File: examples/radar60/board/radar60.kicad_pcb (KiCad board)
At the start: 6 copper layers, 60 x 46 mm, 6 parts

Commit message: radar60 board: Rev A integration, placed by yapnr's Monte Carlo search, not routed
integrate.py combines the schematic's atopile board, the RF macro (rfm1-n) and the floorplan,
runs pnr.mc.halving stage 0 (32 seeded starts), selects mechanically (legal, placement audit,
then the engine's routability proxy, HPWL, id) and writes the board back without routes.
kicad_ops.py merges the macro in U1's frame (copper digest equal to the RF track's board, RF
balls on the macro ports to 0 um), drops the engine's all-layer copper keepouts and the plane
drops writeback adds on its own, and fills the zones; audit.py checks R2, R4, R5, the noise
distances, regions and groups. reva/placement.json records the selected poses; the placed
board (1.2 MB, over the 600 kB limit) is rebuilt from it bit for bit.

Floorplan changes, all derived: RF region, guard and patches follow the calibrated macro; the
VOUT_PA caps go on the bottom under the corner (the macro's pocket holds no 0402 courtyard);
crystal region and HF/bulk decoupling radii widened to what U1's courtyard allows; PMIC block
and J3 region widened; the four mounting holes are the schematic's parts; keepout polygons as
point lists (they were strings) and less U1's courtyard; net classes by pattern in the project.

Co-Authored-By: Claude Opus 5.5 <noreply@anthropic.com>
Claude-Session: https://claude.ai/code/session_014FiHUDEn5jCP4V8pPjQkPy
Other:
- board text added: "pa_corner"
- board text removed: "pa_pocket"

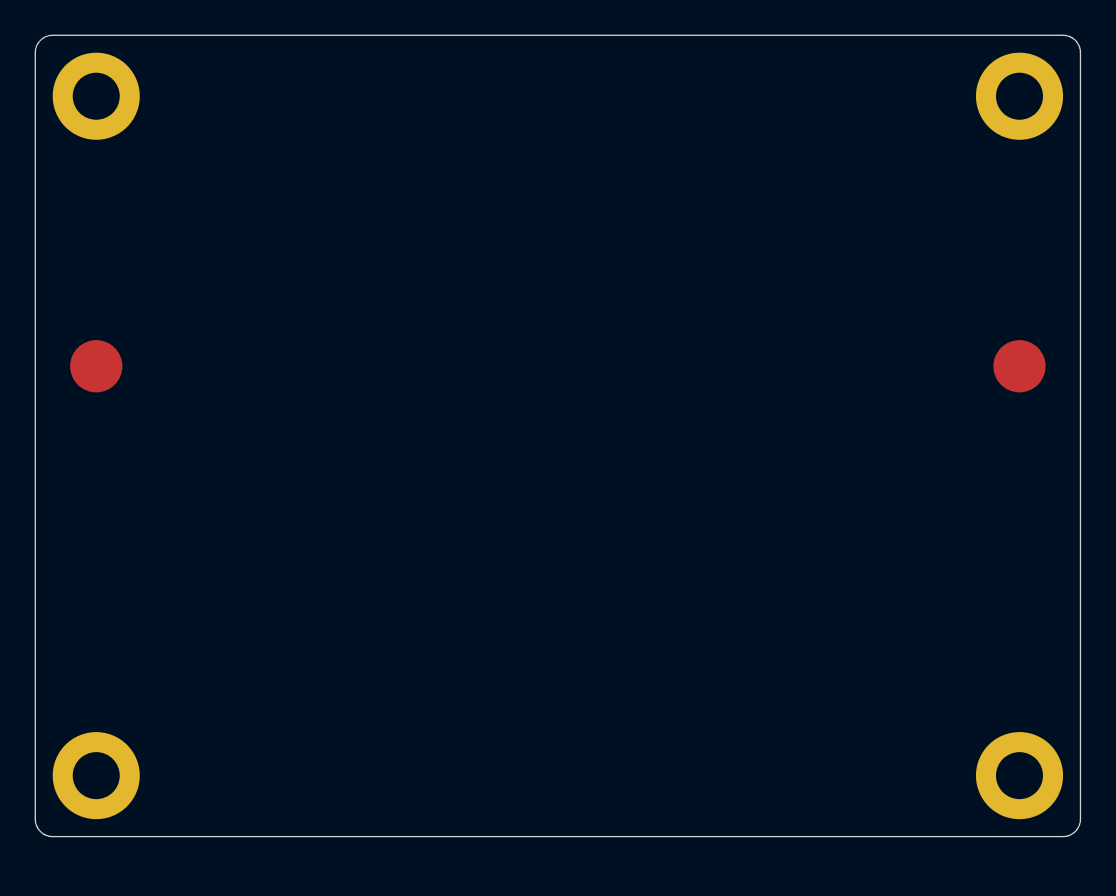
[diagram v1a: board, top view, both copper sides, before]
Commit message: radar60 board: review fixes, ball-anchored decoupling, block groups, re-placed
Adversarial reviews of 735327c (schematic/power and RF/floorplan), fixed on the board side:
- R4: net class ANALOG (VOUT_14*, VBGAP, the eFuse threshold/timer nodes, VIO_LS_ON, DAMP_*,
  PMIC_FB_B2), exempt from radar60_rf_guard_digital like RF/PWR/GND; audit.py and the derived R4
  region now use the rule's own class test (they disagreed on 11 parts). dru_selftest 21/21.
- Ball-anchored parts: U1 is fixed, so the APLL, VBGAP and SYNTH caps, the crystal load caps,
  the VOUT_PA/VIN_13RF2 220 nF and PA 0 ohm (bottom, under the corner) and the QSPI clock
  resistor each get a one-slot region next to their ball and a rotation that turns the signal
  pad toward it: 2.25/3.44/3.07, 2.1/2.3, 0.5-1.1 and 2.1 mm (were up to 12-17 mm). The PA/RF2
  bulk goes on the bottom east of the package (7-12 mm; nearer needs the BGA shadow and E4).
- Blocks: hard groups for the eFuse network, CAN and flash parts, PMIC input caps, snubbers
  (each C within 2.5 mm of its R) and VANA; regions for the block anchors and for the ESD/TVS at
  J1. J2 and J3 are fixed (as region parts the legalizer stranded them behind the blocks).
  audit.py adds pad-to-ball limits and the protection order on J1's lines.
- Outline 60 x 46.3 mm (5.0 mm ground beyond the RX patches); plated GND mounting holes at
  y 42.8; IHLP-1616 inductors in the PMIC block; BGA via rules leave the macro's RF-region vias
  to their own class; gen_board --macro checks all three D12 variants; integrate.py
  --macro-variant.

Re-placed with pnr.mc.halving stage 0 (32 starts, seed 0): 12 legal, all pass the audit,
winner p002 (no unreachable branch). KiCad DRC on the written board: only the unconfigured
footprint libraries (183) and the 432 unrouted connections. finish --placement rebuilds it bit
for bit (sha256 1d342ef4...).

Co-Authored-By: Claude Opus 5.5 <noreply@anthropic.com>
Claude-Session: https://claude.ai/code/session_014FiHUDEn5jCP4V8pPjQkPy
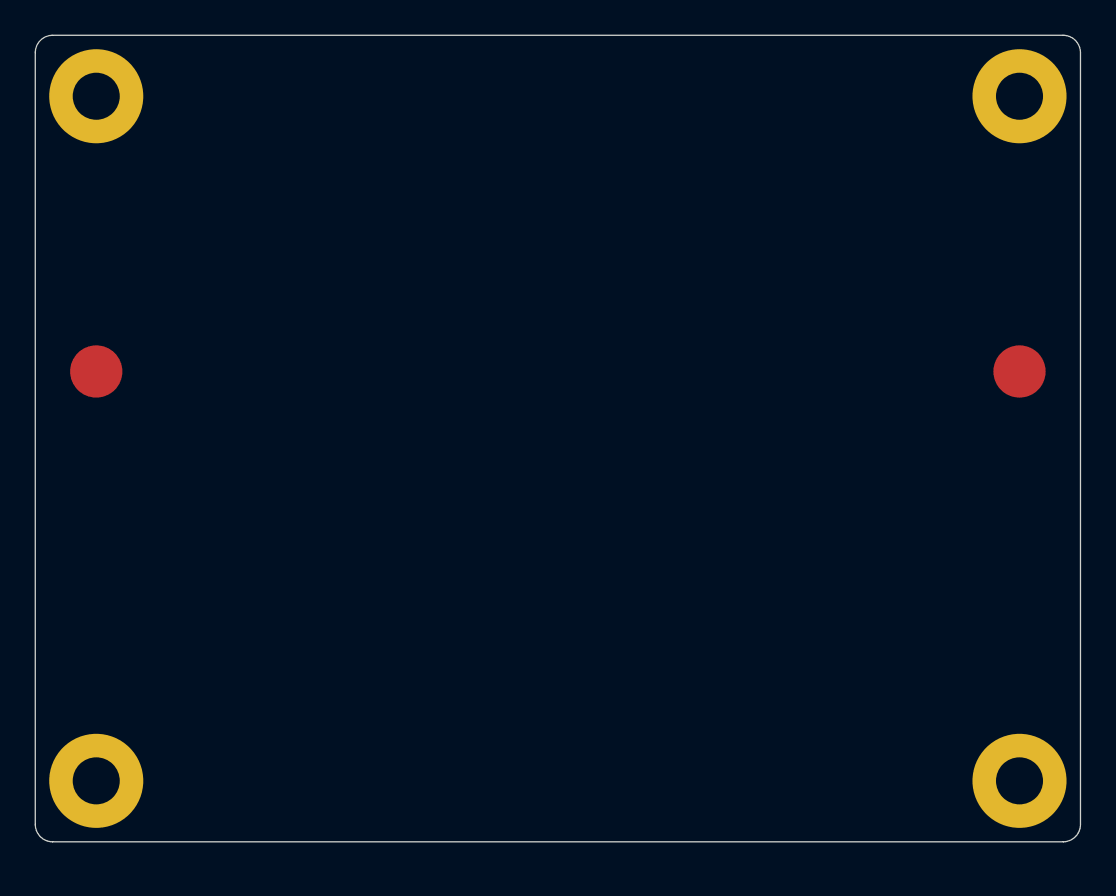
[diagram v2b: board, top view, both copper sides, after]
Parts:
- moved H1 0.30 mm to (33.5, 72.8)
- moved H2 0.30 mm to (86.5, 72.8)
- moved RL1 0.30 mm to (33.5, 49.3)
- moved RL2 0.30 mm to (86.5, 49.3)
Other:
- board size 60 x 46 mm -> 60 x 46.3 mm
- board text added: "can_block"
- board text added: "connector_esd"
- board text added: "connector_tvs"
- board text added: "efuse_block"
- board text added: "flash_block"
- board text added: "pa_bulk"
- board text added: "pa_cap"
- board text added: "pa_r"
- board text added: "qspi_series"
- board text added: "radio_apll"
- board text added: "radio_synth"
- board text added: "radio_vbgap"
- board text added: "radio_west"
- board text added: "rf2_cap"
- board text added: "xtal_cap_n"
- board text added: "xtal_cap_p"
- board text removed: "jtag"
- board text removed: "lvds_header"
- board text removed: "pa_corner"

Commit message: radar60 board: floorplan from the RF macro's board_frame
The RF-uniformity macro put 473 vias and the new TX bank outside the
floorplan's RF region, so `gen_board.py --check --macro` failed. The
floorplan now takes its values from the macro's board_frame:

- board 60 x 47.35 mm, with the top mounting holes at y 43.85;
- the RF region x 12.599-51.469 and the R4 guard x 7.599-56.469;
- the patch extents including the dummy columns;
- the VOUT_PA pocket 29.557-31.25 x 33.2-34.2 (it holds no part; the
  VOUT_PA parts stay on the bottom side).

constraints.yaml and radar60.kicad_pcb are regenerated, and
`gen_board.py --check --macro --compile` passes for rfm1-m/n/p.
reva/ (the placed board) is still the old macro's; stage 3 re-places it.

Co-Authored-By: Claude Opus 5.5 <noreply@anthropic.com>
Claude-Session: https://claude.ai/code/session_014FiHUDEn5jCP4V8pPjQkPy
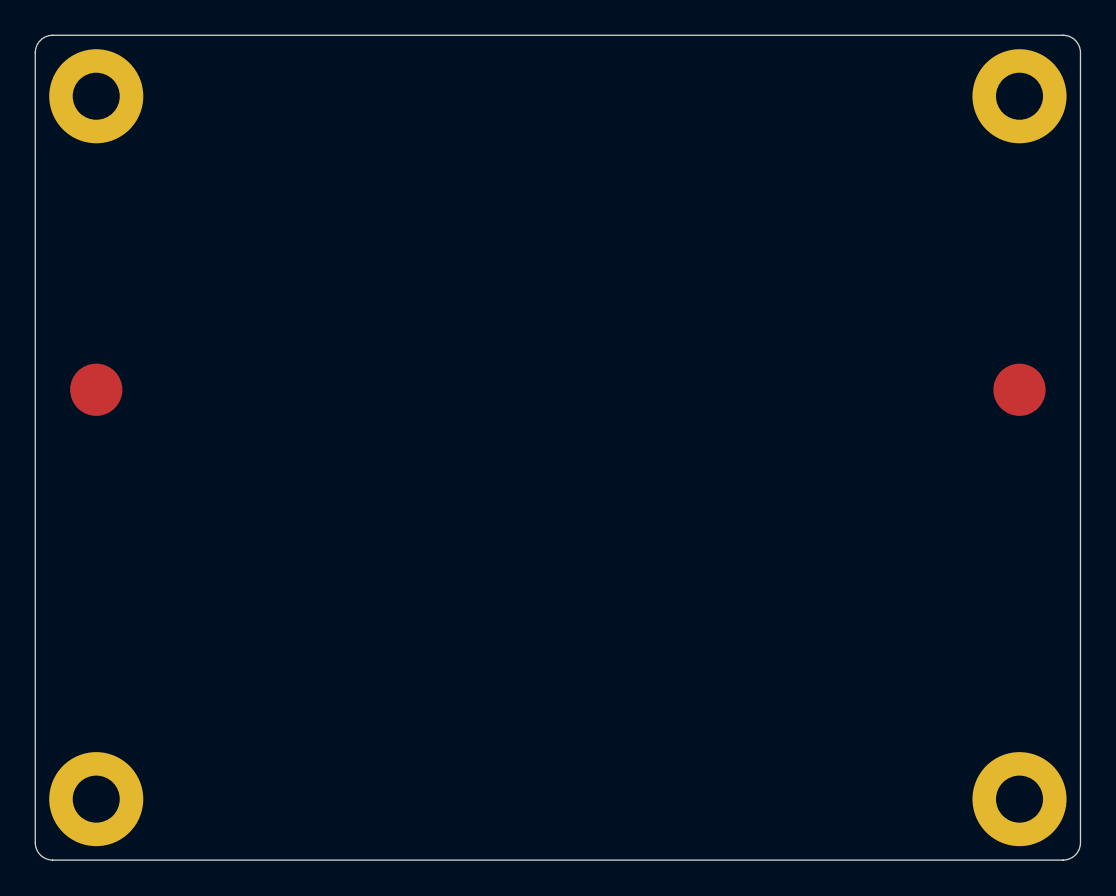
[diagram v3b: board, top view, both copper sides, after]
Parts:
- moved RL1 1.05 mm to (33.5, 50.4)
- moved RL2 1.05 mm to (86.5, 50.4)
- moved H1 1.05 mm to (33.5, 73.8)
- moved H2 1.05 mm to (86.5, 73.8)
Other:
- board size 60 x 46.3 mm -> 60 x 47.3 mm

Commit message: radar60 rf: freeze macro v2 (stage 3b): C1 column pick, rfm1-m/n/p, coupons, board_frame
- rfmacro params: the C1 rule's pick (embedded centre column, cell-c1b-6, K0, 20 um):
  fullwave_l_scale 1.025, inset 0.325, w35 0.42, t_y 0.25. Worst in-band |S11| -6.5 dB
  (-7.2 dB Palace-referred); ANT-02 RL miss preregistered. K1 at L 1.00/1.015/1.03
  (s3b-e3) never reaches -10 dB (best -8.8 dB), so K0 stays per the K rule.
- regenerated rfm1-m/-n/-p and coupons with the frozen defaults (S1 outer dummies, D14 PA
  feed + fence, D15 A, C1); KiCad DRC 0 violations, 0 unconnected on all three.
- board/floorplan.yaml follows the new board_frame: height 47.40 (min 47.384), patches,
  region, pocket (now 1.69 x 1.55), guard, mounting holes; gen_board --macro all covered.
- tests: expectations updated for the S1 default (were failing at HEAD since the S1/fence
  freeze); series/T4 option tests pin S2 dummies (under S1 they leave a G4 fence gap).

Co-Authored-By: Claude Opus 5.5 <noreply@anthropic.com>
Claude-Session: https://claude.ai/code/session_01XmUgXgxLjzBpn2W6JpqE2p
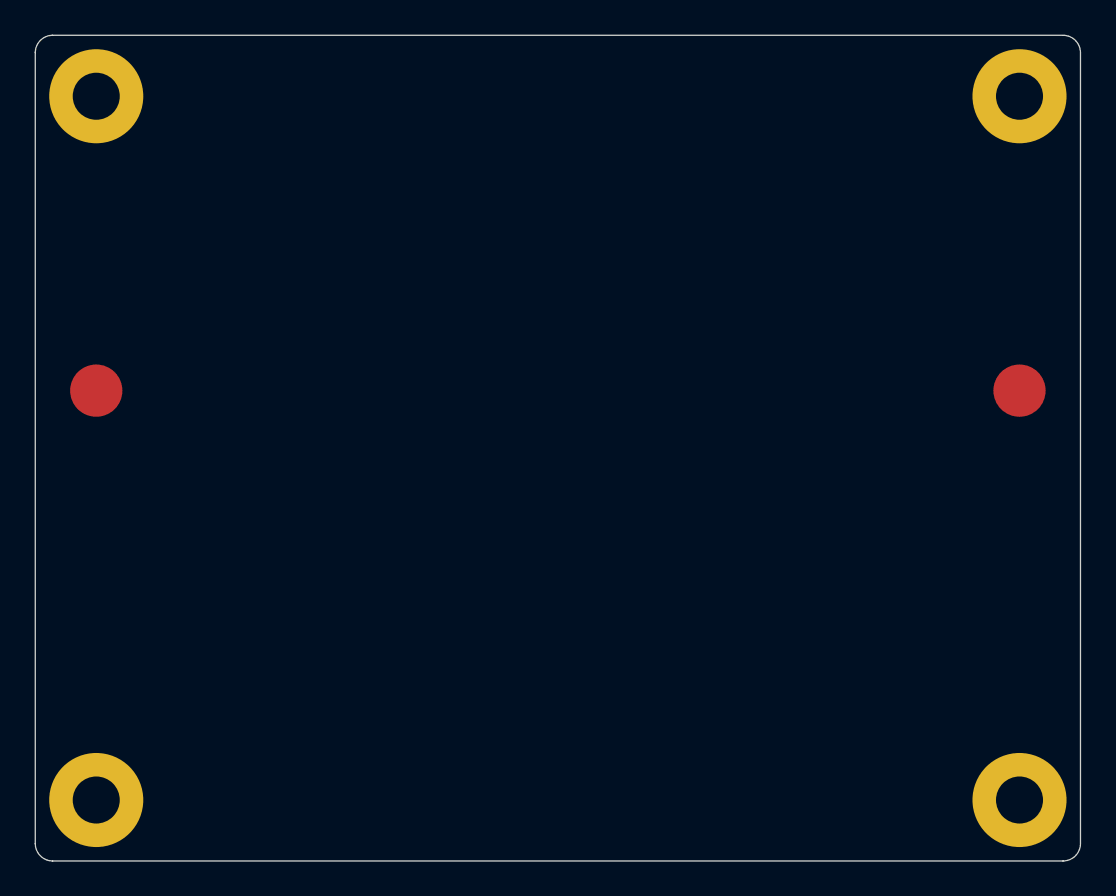
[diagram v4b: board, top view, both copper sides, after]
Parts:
- moved H1 0.05 mm to (33.5, 73.9)
- moved H2 0.05 mm to (86.5, 73.9)
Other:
- board size 60 x 47.3 mm -> 60 x 47.4 mm
